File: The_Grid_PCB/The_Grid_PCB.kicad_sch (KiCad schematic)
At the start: 26 parts, among them J9 Screw_Terminal_01x02, U1 STM32F030C8Tx, U2 XL1509-3.3, U3 SN65HVD11HD, X1 X322516MLB4SI

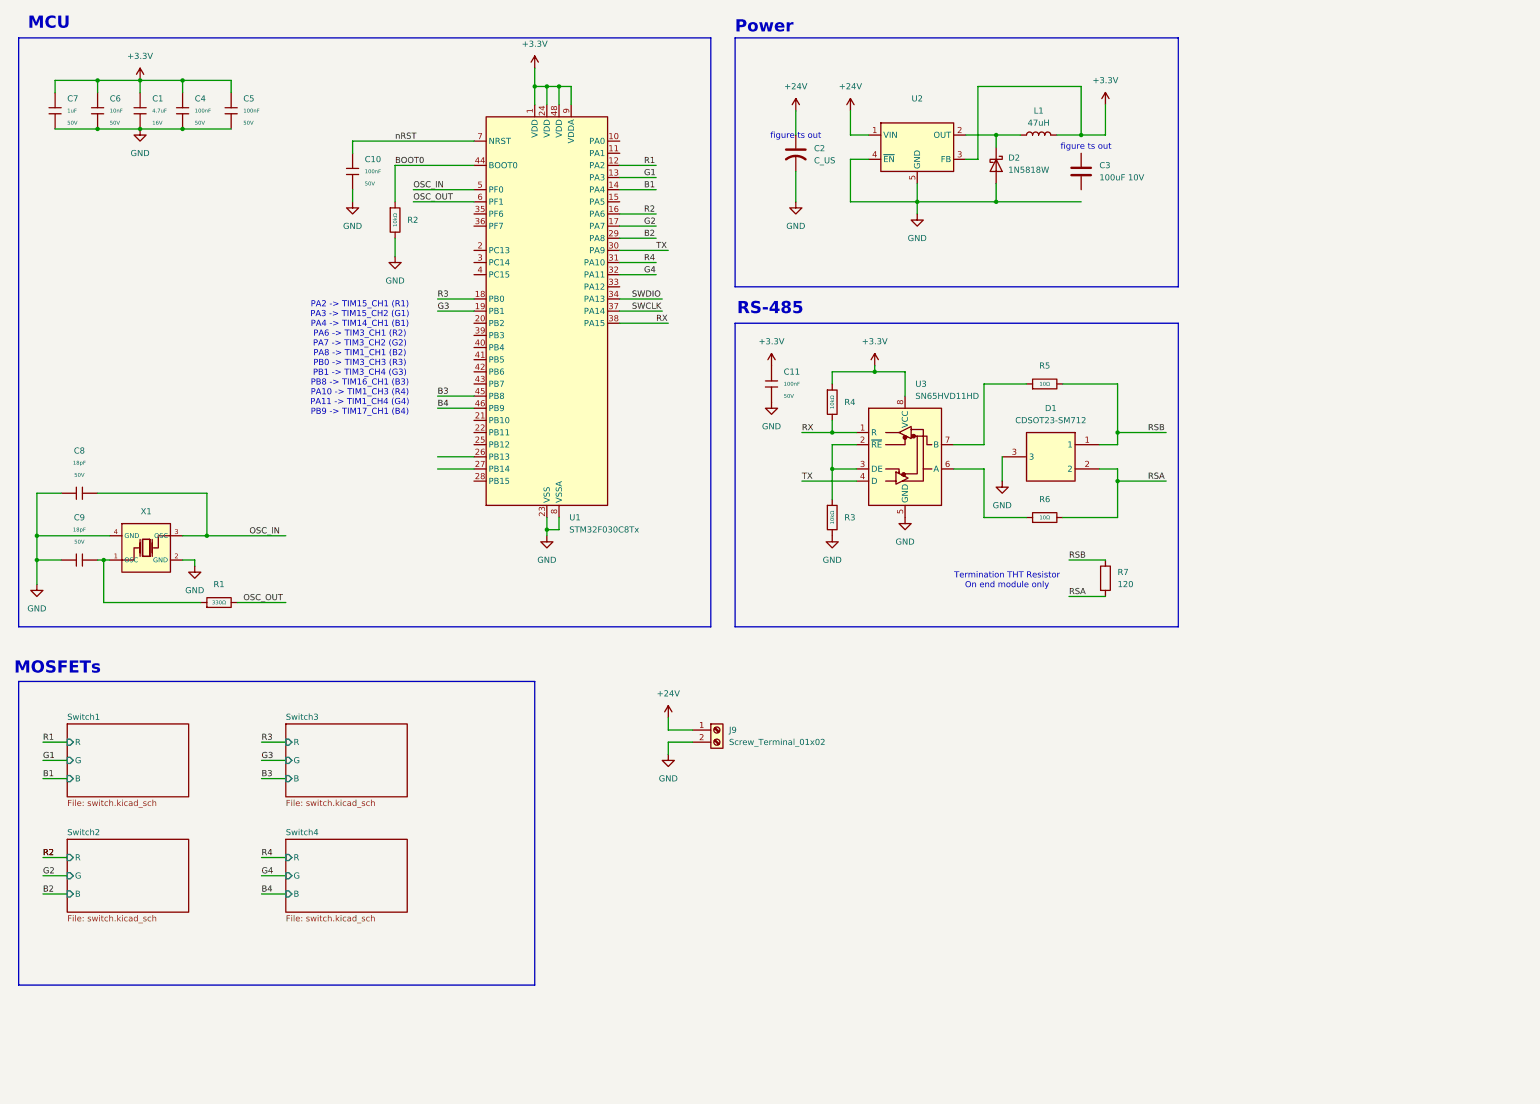
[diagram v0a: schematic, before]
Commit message: update custom symbols
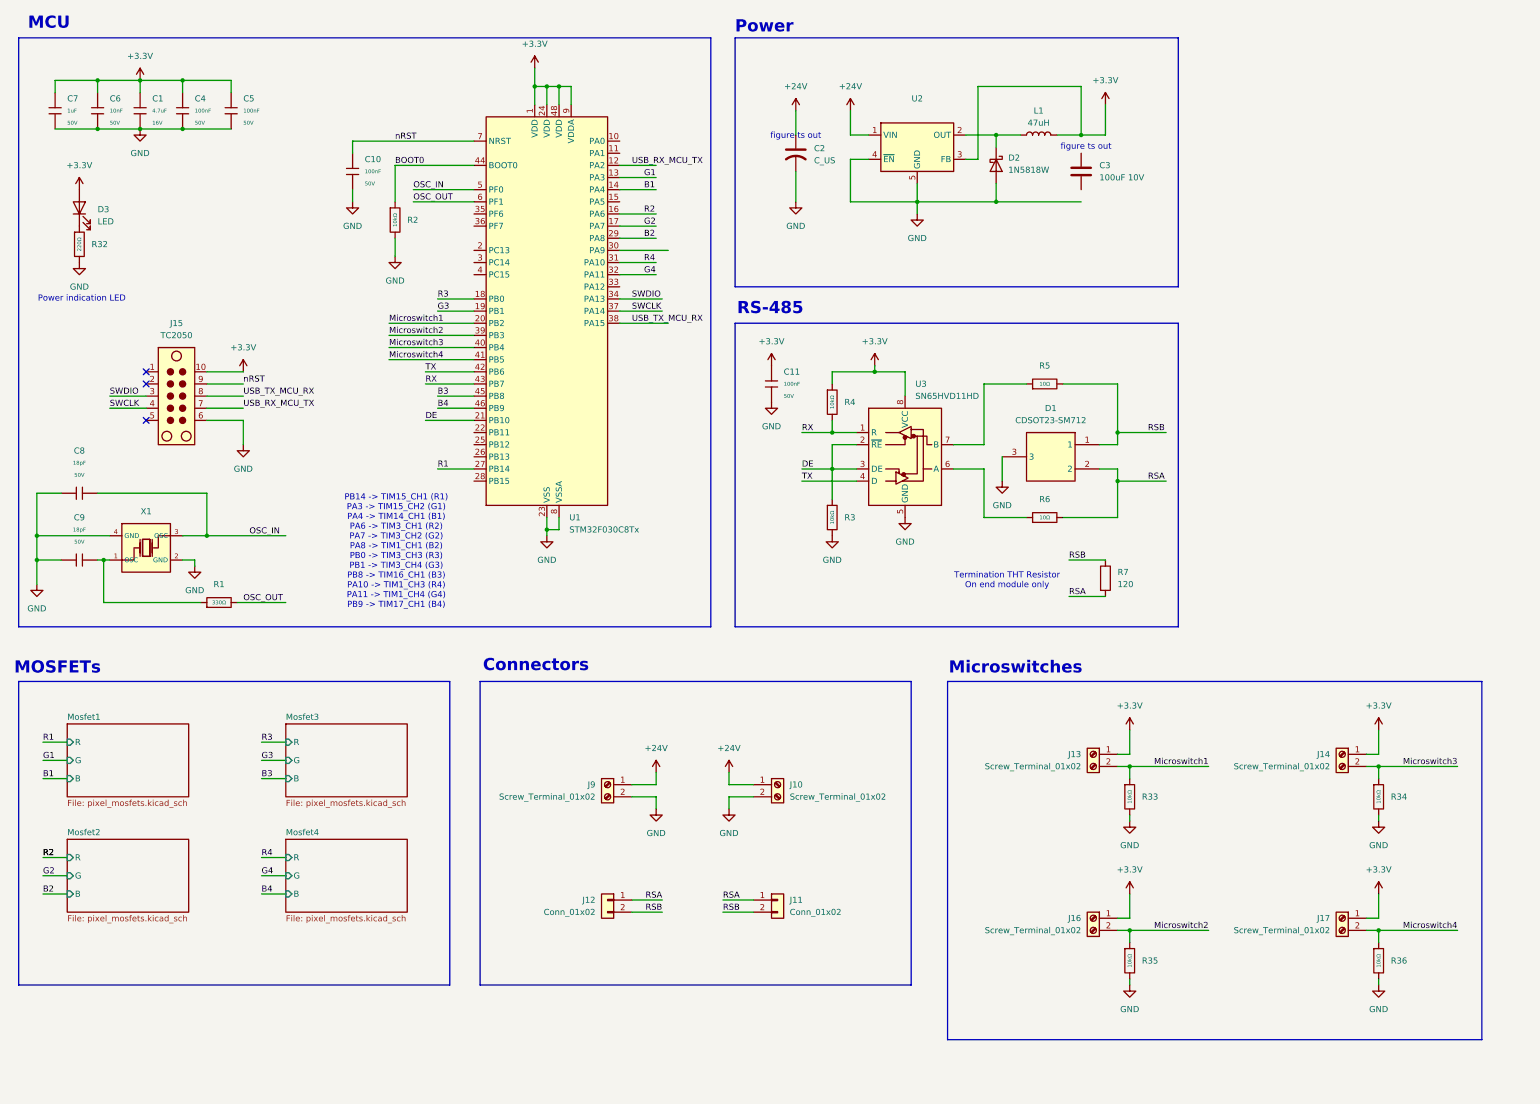
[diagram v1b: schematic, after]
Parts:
- added D3: LED, LED_SMD:LED_0805_2012Metric_Pad1.15x1.40mm_HandSolder, symbol Device:LED
- added J10, J13, J14, J16, J17: Screw_Terminal_01x02, TerminalBlock_4Ucon:TerminalBlock_4Ucon_1x02_P3.50mm_Vertical, symbol Connector:Screw_Terminal_01x02
- added J11, J12: Conn_01x02, Connector_JST:JST_XH_B2B-XH-A_1x02_P2.50mm_Vertical, symbol Connector_Generic:Conn_01x02
- added J15: TC2050, Connector:Tag-Connect_TC2070-IDC-FP_2x07_P1.27mm_Vertical, symbol Connector:TC2050
- added R32: 220Ω, PCM_JLCPCB:R_0603, symbol PCM_JLCPCB-Resistors:0603,220Ω
- added R33, R34, R35, R36: 10kΩ, PCM_JLCPCB:R_0603, symbol PCM_JLCPCB-Resistors:0603,10kΩ
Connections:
- net +24V: now also J10.1 (Pin_1)
- net +3.3V: now also D3.2 (A), J13.1 (Pin_1), J14.1 (Pin_1), J15.10, J16.1 (Pin_1), J17.1 (Pin_1)
- net GND: now also J10.2 (Pin_2), J15.6, R32.2, R33.2, R34.2, R35.2, R36.2
- net R1: now also U1.27 (PB14); no longer U1.12 (PA2)
- net RSA: now also J11.1 (Pin_1), J12.1 (Pin_1)
- net RSB: now also J11.2 (Pin_2), J12.2 (Pin_2)
- net RX: now also U1.43 (PB7); no longer U1.38 (PA15)
- net SWCLK: now also J15.4
- net SWDIO: now also J15.3
- net TX: now also U1.42 (PB6); no longer U1.30 (PA9)
- net nRST: now also J15.9
- net DE: now reaches R3.1, U3.2 (~{RE}), U3.3 (DE)
- net DE: now also U1.21 (PB10)
- net Microswitch1: now reaches U1.20 (PB2)
- net Microswitch1: now also J13.2 (Pin_2), R33.1
- net Microswitch2: now reaches U1.39 (PB3)
- net Microswitch2: now also J16.2 (Pin_2), R35.1
- net Microswitch3: now reaches U1.40 (PB4)
- net Microswitch3: now also J14.2 (Pin_2), R34.1
- net Microswitch4: now reaches U1.41 (PB5)
- net Microswitch4: now also J17.2 (Pin_2), R36.1
- new net: D3.1 (K), R32.1
- new net USB_RX_MCU_TX: J15.7, U1.12 (PA2)
- new net USB_TX_MCU_RX: J15.8, U1.38 (PA15)
- no-connect marks 0 -> 3
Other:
- sheet Switch1 renamed Mosfet1
- removed sheet Switch2
- removed sheet Switch3
- removed sheet Switch4
- added sheet Mosfet2 (pixel_mosfets.kicad_sch)
- added sheet Mosfet3 (pixel_mosfets.kicad_sch)
- added sheet Mosfet4 (pixel_mosfets.kicad_sch)
- sheet Mosfet1: file switch.kicad_sch -> pixel_mosfets.kicad_sch
- note added: "Connectors"
- note added: "Microswitches"
- note added: "PB14 -> TIM15_CH1 (R1) PA3 -> TIM15_CH2 (G1) PA4 -> TIM14_CH1 (B1) PA6 -> TIM3_CH1 (R2) PA7 -> TIM3_CH2 (G2) PA8 -> TIM1_CH1 (B2) PB0 -> TIM3_CH3 (R3) PB1 -> TIM3_CH4 (G3) PB8 -> TIM16_CH1 (B3) PA10 -> TIM1_CH3 (R4) PA11 -> TIM1_CH4 (G4) PB9 -> TIM17_CH1 (B4)"
- note added: "Power indication LED"
- note removed: "PA2 -> TIM15_CH1 (R1) PA3 -> TIM15_CH2 (G1) PA4 -> TIM14_CH1 (B1) PA6 -> TIM3_CH1 (R2) PA7 -> TIM3_CH2 (G2) PA8 -> TIM1_CH1 (B2) PB0 -> TIM3_CH3 (R3) PB1 -> TIM3_CH4 (G3) PB8 -> TIM16_CH1 (B3) PA10 -> TIM1_CH3 (R4) PA11 -> TIM1_CH4 (G4) PB9 -> TIM17_CH1 (B4)"
- moved on the sheet: J9

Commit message: draft 1 schematic
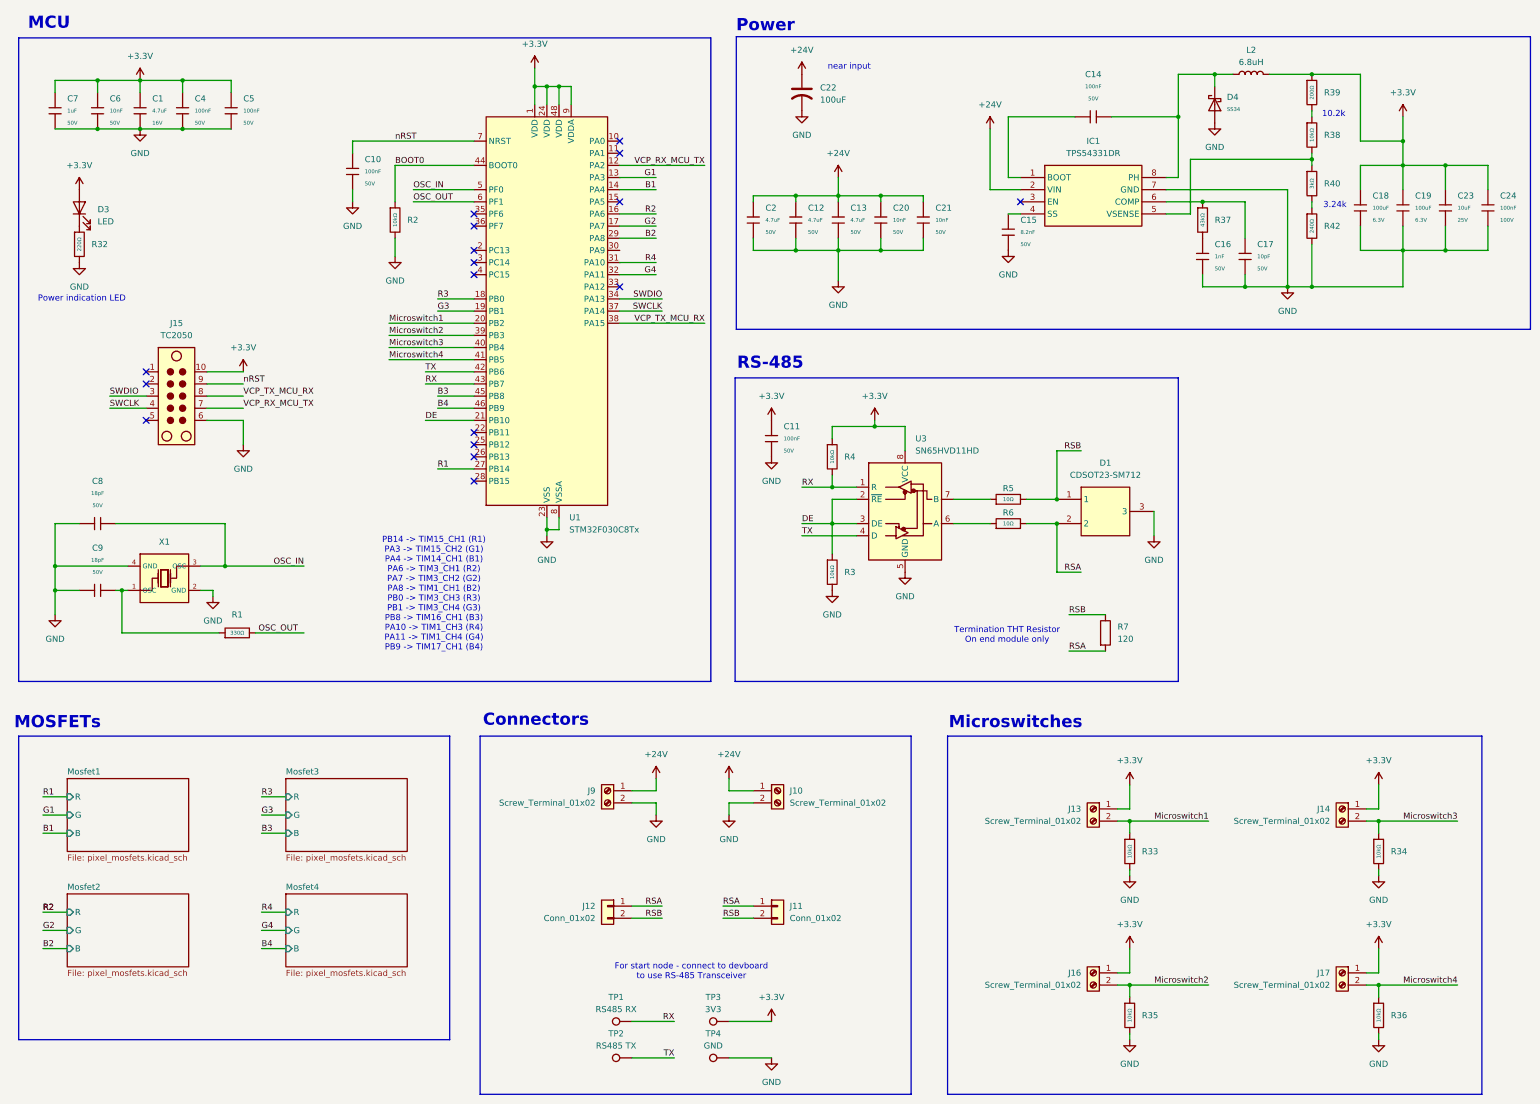
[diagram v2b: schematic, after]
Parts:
- removed C2: C_US, symbol Device:C_US
- removed C3: 100uF 10V, Capacitor_SMD:C_1206_3216Metric, symbol Device:C
- removed D2: 1N5818W, PCM_JLCPCB:D_SOD-123FL, symbol Diode:1N5818
- removed L1: 47uH, Inductor_SMD:L_Ferrocore_DLG-0403, symbol Device:L
- removed U2: XL1509-3.3, Package_SO:SOIC-8_3.9x4.9mm_P1.27mm, symbol Regulator_Switching:XL1509-3.3
- added C12, C13, C2: 4.7uF, PCM_JLCPCB:C_1206, symbol PCM_JLCPCB-Capacitors:1206,4.7uF
- added C14: 100nF, PCM_JLCPCB:C_0603, symbol PCM_JLCPCB-Capacitors:0603,100nF
- added C15: 8.2nF, PCM_JLCPCB:C_0603, symbol PCM_JLCPCB-Capacitors:0603,8.2nF
- added C16: 1nF, PCM_JLCPCB:C_0805, symbol PCM_JLCPCB-Capacitors:0805,1nF
- added C17: 10pF, PCM_JLCPCB:C_0603, symbol PCM_JLCPCB-Capacitors:0603,10pF
- added C18, C19: 100uF, PCM_JLCPCB:C_1206, symbol PCM_JLCPCB-Capacitors:1206,100uF
- added C20, C21: 10nF, PCM_JLCPCB:C_0805, symbol PCM_JLCPCB-Capacitors:0805,10nF
- added C22: 100uF, Capacitor_THT:CP_Radial_D8.0mm_P3.50mm, symbol Device:C_US
- added C23: 10uF, PCM_JLCPCB:C_0805, symbol PCM_JLCPCB-Capacitors:0805,10uF
- added C24: 100nF, PCM_JLCPCB:C_0805, symbol PCM_JLCPCB-Capacitors:0805,100nF
- added D4: SS34, PCM_JLCPCB:D_SMA, symbol PCM_JLCPCB-Diodes:Schottky,SS34
- added IC1: TPS54331DR, TPS54331DR:SOIC127P600X175-8N, symbol TPS54331DR:TPS54331DR
- added L2: 6.8uH, Inductor_SMD:L_Sumida_CDMC6D28_7.25x6.5mm, symbol Device:L
- added R37: 43kΩ, PCM_JLCPCB:R_0603, symbol PCM_JLCPCB-Resistors:0603,43kΩ
- added R38: 10kΩ, PCM_JLCPCB:R_0603, symbol PCM_JLCPCB-Resistors:0603,10kΩ
- added R39: 200Ω, PCM_JLCPCB:R_0603, symbol PCM_JLCPCB-Resistors:0603,200Ω
- added R40: 3kΩ, PCM_JLCPCB:R_0603, symbol PCM_JLCPCB-Resistors:0603,3kΩ
- added R42: 240Ω, PCM_JLCPCB:R_0603, symbol PCM_JLCPCB-Resistors:0603,240Ω
- added TP1: RS485 RX, TestPoint:TestPoint_THTPad_D2.0mm_Drill1.0mm, symbol Connector:TestPoint
- added TP2: RS485 TX, TestPoint:TestPoint_THTPad_D2.0mm_Drill1.0mm, symbol Connector:TestPoint
- added TP3: 3V3, TestPoint:TestPoint_THTPad_D2.0mm_Drill1.0mm, symbol Connector:TestPoint
- added TP4: GND, TestPoint:TestPoint_THTPad_D2.0mm_Drill1.0mm, symbol Connector:TestPoint
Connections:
- net +24V: now also C12.1, C13.1, C2.1, C20.1, C21.1, C22.1, IC1.2 (VIN)
- net +3.3V: now also C18.1, C19.1, C23.1, C24.1, L2.2, R39.1, TP3.1
- net GND: now also C12.2, C13.2, C15.2, C16.2, C17.2, C18.2, C19.2, C2.2, C20.2, C21.2, C22.2, C23.2, C24.2, D4.2, IC1.7 (GND), R42.2, TP4.1
- net RX: now also TP1.1
- net TX: now also TP2.1
- net USB_RX_MCU_TX renamed VCP_RX_MCU_TX
- net USB_TX_MCU_RX renamed VCP_TX_MCU_RX
- new net: C14.2, D4.1, IC1.8 (PH), L2.1
- new net: R38.1, R39.2
- new net: IC1.5 (VSENSE), R38.2, R40.1
- new net: C14.1, IC1.1 (BOOT)
- new net: C15.1, IC1.4 (SS)
- new net: C17.1, IC1.6 (COMP), R37.1
- new net: R40.2, R42.1
- new net: C16.1, R37.2
- no-connect marks 3 -> 17
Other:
- note added: "10.2k"
- note added: "3.24k"
- note added: "For start node - connect to devboard to use RS-485 Transceiver"
- note added: "near input"
- note removed: "figure ts out"
- moved on the sheet: C11, C8, C9, D1, J10, J11, J12, J13, J14, J16, J17, J9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

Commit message: pcb iter 1 done
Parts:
- removed C21: 10nF, PCM_JLCPCB:C_0805, symbol PCM_JLCPCB-Capacitors:0805,10nF
- removed D1: CDSOT23-SM712, Package_TO_SOT_SMD:SOT-23, symbol CDSOT23-SM712:CDSOT23-SM712
- removed J10, J9: Screw_Terminal_01x02, TerminalBlock_4Ucon:TerminalBlock_4Ucon_1x02_P3.50mm_Vertical, symbol Connector:Screw_Terminal_01x02
- added D2: CDSOT23-SM712, Package_TO_SOT_SMD:SOT-23, symbol CDSOT23-SM712:CDSOT23-SM712
- added J2, J5: Screw_Terminal_01x02, TerminalBlock:TerminalBlock_MaiXu_MX126-5.0-02P_1x02_P5.00mm, symbol Connector:Screw_Terminal_01x02
- C12: renamed from C22; LCSC (none) -> C112510
- D1: renamed from D3; footprint LED_SMD:LED_0805_2012Metric_Pad1.15x1.40mm_HandSolder -> PCM_JLCPCB:D_0603; LCSC (none) -> C2286
- J1: renamed from J15; now not fitted
- J3: renamed from J11; footprint Connector_JST:JST_XH_B2B-XH-A_1x02_P2.50mm_Vertical -> james_custom_footprint_library:JST_XH_B02B-XH-A_02x2.50mm_7.32x7.5_RightAngle; LCSC (none) -> C47326862
- J4: renamed from J12; footprint Connector_JST:JST_XH_B2B-XH-A_1x02_P2.50mm_Vertical -> james_custom_footprint_library:JST_XH_B02B-XH-A_02x2.50mm_7.32x7.5_RightAngle; LCSC (none) -> C47326862
- J6: renamed from J13; footprint TerminalBlock_4Ucon:TerminalBlock_4Ucon_1x02_P3.50mm_Vertical -> TerminalBlock_4Ucon:TerminalBlock_4Ucon_1x02_P3.50mm_Horizontal; LCSC (none) -> C695629
- J7: renamed from J16; footprint TerminalBlock_4Ucon:TerminalBlock_4Ucon_1x02_P3.50mm_Vertical -> TerminalBlock_4Ucon:TerminalBlock_4Ucon_1x02_P3.50mm_Horizontal; LCSC (none) -> C695629
- J8: renamed from J14; footprint TerminalBlock_4Ucon:TerminalBlock_4Ucon_1x02_P3.50mm_Vertical -> TerminalBlock_4Ucon:TerminalBlock_4Ucon_1x02_P3.50mm_Horizontal; LCSC (none) -> C695629
- J9: renamed from J17; footprint TerminalBlock_4Ucon:TerminalBlock_4Ucon_1x02_P3.50mm_Vertical -> TerminalBlock_4Ucon:TerminalBlock_4Ucon_1x02_P3.50mm_Horizontal; LCSC (none) -> C695629
- L1: renamed from L2; LCSC (none) -> C5189749
- R8: renamed from R7; now not fitted
- U1: LCSC (none) -> C23922
- U2: renamed from U3; LCSC (none) -> C68886
- U3: renamed from IC1; LCSC (none) -> C9865
- renumbered C7 to C1, C11 to C10, C12 to C11, C20 to C14, C14 to C16, C16 to C17, C17 to C18, C18 to C19, C6 to C2, C19 to C20, C23 to C21, C24 to C22, C8 to C3, C9 to C4, C1 to C5, C4 to C6, C5 to C7, C10 to C8, C2 to C9, D4 to D3, R32 to R1, R35 to R10, R37 to R11, R39 to R12, R38 to R13, R40 to R14, R42 to R15, R34 to R16, R36 to R17, R1 to R2, R2 to R3, R3 to R5, R5 to R6, R6 to R7, R33 to R9
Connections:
- net +24V: now also J2.1 (Pin_1), J5.2 (Pin_2)
- net B1: now also U1.13 (PA3); no longer U1.14 (PA4)
- net B2: now also U1.17 (PA7); no longer U1.29 (PA8)
- net B3: now also U1.32 (PA11); no longer U1.45 (PB8)
- net B4: now also U1.27 (PB14); no longer U1.46 (PB9)
- net G1: now also U1.46 (PB9); no longer U1.13 (PA3)
- net G2: now also U1.16 (PA6); no longer U1.17 (PA7)
- net G3: now also U1.31 (PA10); no longer U1.19 (PB1)
- net G4: now also U1.19 (PB1); no longer U1.32 (PA11)
- net GND: now also D2.3, J2.2 (Pin_2), J5.1 (Pin_1)
- net Microswitch2: now also U1.41 (PB5); no longer U1.39 (PB3)
- net Microswitch4: now also U1.39 (PB3); no longer U1.41 (PB5)
- net R1: now also U1.45 (PB8); no longer U1.27 (PB14)
- net R2: now also U1.14 (PA4); no longer U1.16 (PA6)
- net R3: now also U1.29 (PA8); no longer U1.18 (PB0)
- net R4: now also U1.18 (PB0); no longer U1.31 (PA10)
- net RSA: now also J4.2 (Pin_2), D2.1; no longer J4.1 (Pin_1)
- net RSB: now also J4.1 (Pin_1), D2.2; no longer J4.2 (Pin_2)
- no-connect marks 17 -> 18
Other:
- note added: "PB8 -> TIM16_CH1 (R1) PB9 -> TIM17_CH1 (G1) PA3 -> TIM15_CH2 (B1) PA4 -> TIM14_CH1 (R2) PA6 -> TIM3_CH1 (G2) PA7 -> TIM3_CH2 (B2) PA8 -> TIM1_CH1 (R3) PA10 -> TIM1_CH3 (G3) PA11 -> TIM1_CH4 (B3) PB0 -> TIM3_CH3 (R4) PB1 -> TIM3_CH4 (G4) PB14 -> TIM15_CH1 (B4)"
- note removed: "PB14 -> TIM15_CH1 (R1) PA3 -> TIM15_CH2 (G1) PA4 -> TIM14_CH1 (B1) PA6 -> TIM3_CH1 (R2) PA7 -> TIM3_CH2 (G2) PA8 -> TIM1_CH1 (B2) PB0 -> TIM3_CH3 (R3) PB1 -> TIM3_CH4 (G3) PB8 -> TIM16_CH1 (B3) PA10 -> TIM1_CH3 (R4) PA11 -> TIM1_CH4 (G4) PB9 -> TIM17_CH1 (B4)"
- moved on the sheet: J3, J4, R6, R7
